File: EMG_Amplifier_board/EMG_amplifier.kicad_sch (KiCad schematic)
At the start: 0 parts

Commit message: add footprints
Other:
- sheet LPF_400Hz ports: added GND; removed none
- sheet first_amp_stage ports: added GND, V_DD/2; removed none
- sheet input_protection_and_decoupling ports: added GND; removed none
- sheet output_protection ports: added GND; removed none

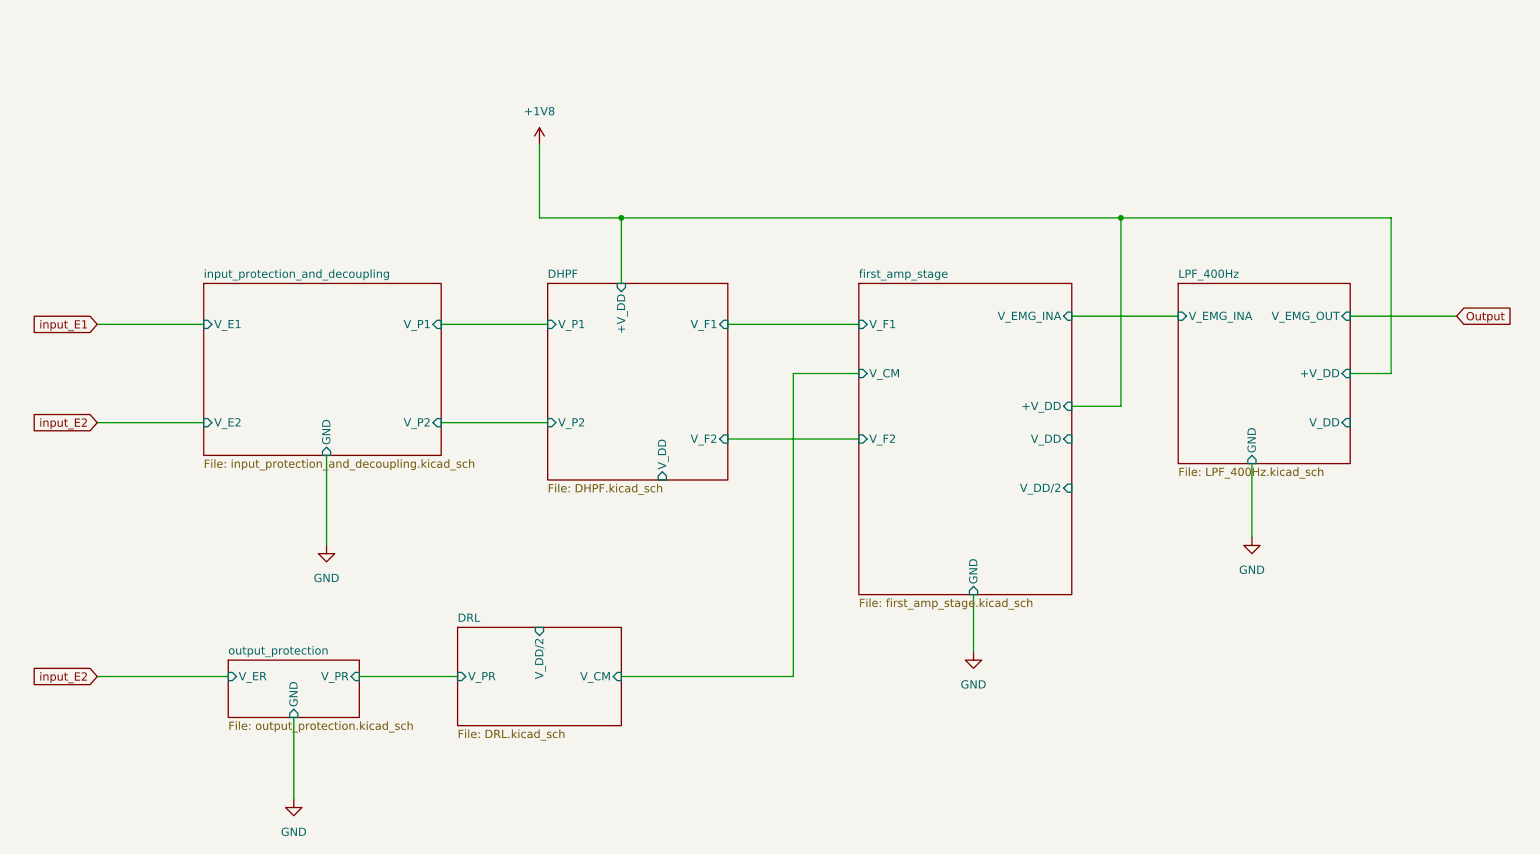
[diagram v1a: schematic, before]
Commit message: update the schematic with shared grounds and pin connectors
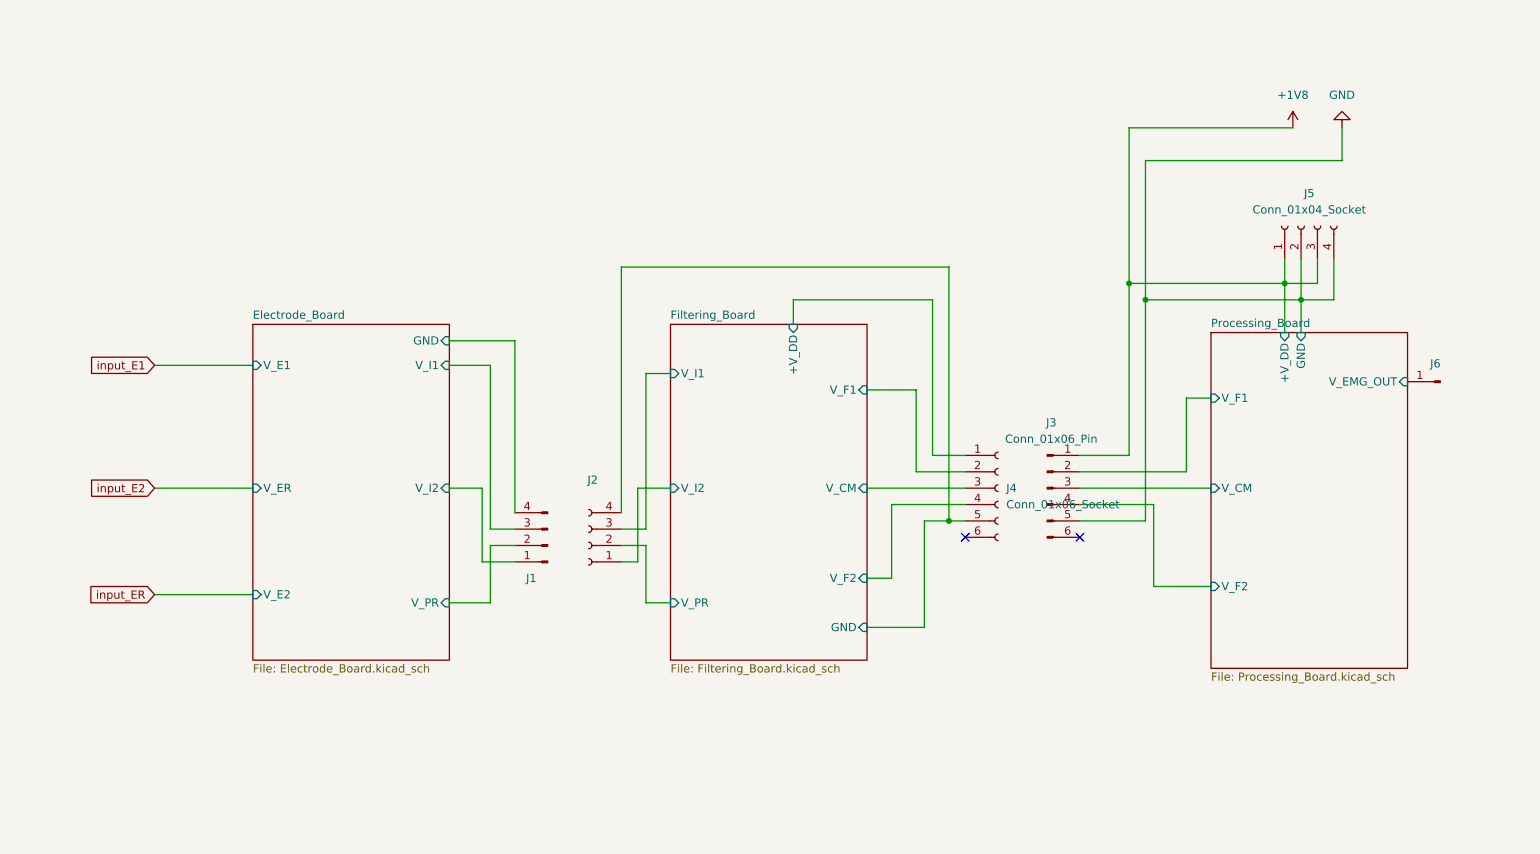
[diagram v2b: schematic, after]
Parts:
- added J1: Conn_01x04_Pin, Connector_PinSocket_2.54mm:PinSocket_2x02_P2.54mm_Vertical, symbol Connector:Conn_01x04_Pin
- added J2, J5: Conn_01x04_Socket, Connector_PinSocket_2.54mm:PinSocket_2x02_P2.54mm_Vertical, symbol Connector:Conn_01x04_Socket
- added J3: Conn_01x06_Pin, Connector_PinHeader_2.54mm:PinHeader_2x03_P2.54mm_Vertical, symbol Connector:Conn_01x06_Pin
- added J4: Conn_01x06_Socket, Connector_PinSocket_2.54mm:PinSocket_2x03_P2.54mm_Vertical, symbol Connector:Conn_01x06_Socket
- added J6: Conn_01x01_Pin, symbol Connector:Conn_01x01_Pin
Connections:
- net +1V8: now also J3.1 (Pin_1), J5.1 (Pin_1), J5.3 (Pin_3)
- net GND: now also J3.5 (Pin_5), J5.2 (Pin_2), J5.4 (Pin_4)
- new net Electrode_Board/GND: J1.4 (Pin_4)
- new net Electrode_Board/V_I1: J1.3 (Pin_3)
- new net Electrode_Board/V_I2: J1.1 (Pin_1)
- new net Electrode_Board/V_PR: J1.2 (Pin_2)
- new net Filtering_Board/+V_DD: J4.1 (Pin_1)
- new net Filtering_Board/GND: J2.4 (Pin_4), J4.5 (Pin_5)
- new net Filtering_Board/V_CM: J4.3 (Pin_3)
- new net Filtering_Board/V_F1: J4.2 (Pin_2)
- new net Filtering_Board/V_F2: J4.4 (Pin_4)
- new net Filtering_Board/V_I1: J2.3 (Pin_3)
- new net Filtering_Board/V_I2: J2.1 (Pin_1)
- new net Filtering_Board/V_PR: J2.2 (Pin_2)
- new net Processing_Board/V_CM: J3.3 (Pin_3)
- new net Processing_Board/V_EMG_OUT: J6.1 (Pin_1)
- new net Processing_Board/V_F1: J3.2 (Pin_2)
- new net Processing_Board/V_F2: J3.4 (Pin_4)
- no-connect marks 0 -> 2
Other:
- removed sheet DHPF
- removed sheet DRL
- removed sheet LPF_400Hz
- removed sheet first_amp_stage
- removed sheet input_protection_and_decoupling
- removed sheet output_protection
- added sheet Electrode_Board (Electrode_Board.kicad_sch)
- added sheet Filtering_Board (Filtering_Board.kicad_sch)
- added sheet Processing_Board (Processing_Board.kicad_sch)

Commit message: pcb design v1
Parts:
- removed J1: Conn_01x04_Pin, Connector_PinSocket_2.54mm:PinSocket_2x02_P2.54mm_Vertical, symbol Connector:Conn_01x04_Pin
- removed J2, J5: Conn_01x04_Socket, Connector_PinSocket_2.54mm:PinSocket_2x02_P2.54mm_Vertical, symbol Connector:Conn_01x04_Socket
- added J1: Conn_01x04_Socket, Connector_PinSocket_2.54mm:PinSocket_2x02_P2.54mm_Vertical, symbol Connector:Conn_01x04_Socket
- added J2: Conn_01x04_Pin, Connector_PinSocket_2.54mm:PinSocket_2x02_P2.54mm_Vertical, symbol Connector:Conn_01x04_Pin
- added J5: Conn_01x04_Pin, Connector_PinHeader_2.54mm:PinHeader_2x02_P2.54mm_Vertical, symbol Connector:Conn_01x04_Pin
- J6: footprint (none) -> Connector_PinHeader_2.54mm:PinHeader_1x01_P2.54mm_Vertical
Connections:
- net Filtering_Board/GND is gone; now on net GND: J4.5 (Pin_5)
- net +1V8: now also J5.2 (Pin_2), J5.4 (Pin_4)
- net Electrode_Board/V_I1: now also J1.2 (Pin_2)
- net Electrode_Board/V_I2: now also J1.4 (Pin_4)
- net Electrode_Board/V_PR: now also J1.3 (Pin_3)
- net Filtering_Board/V_I1: now also J2.2 (Pin_2)
- net Filtering_Board/V_I2: now also J2.4 (Pin_4)
- net Filtering_Board/V_PR: now also J2.3 (Pin_3)
- net GND: now also J1.1 (Pin_1), J2.1 (Pin_1), J5.1 (Pin_1), J5.3 (Pin_3)
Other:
- sheet Electrode_Board ports: added none; removed GND
- sheet Filtering_Board ports: added none; removed GND

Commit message: before working on one-sided design
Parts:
- removed J5: Conn_01x04_Pin, Connector_PinHeader_2.54mm:PinHeader_2x02_P2.54mm_Vertical, symbol Connector:Conn_01x04_Pin
- removed J6: Conn_01x01_Pin, Connector_PinHeader_2.54mm:PinHeader_1x01_P2.54mm_Vertical, symbol Connector:Conn_01x01_Pin
- added J7: Conn_01x06_Pin, Connector_PinHeader_2.54mm:PinHeader_2x03_P2.54mm_Vertical, symbol Connector:Conn_01x06_Pin
- J2: footprint Connector_PinSocket_2.54mm:PinSocket_2x02_P2.54mm_Vertical -> Connector_PinHeader_2.54mm:PinHeader_2x02_P2.54mm_Vertical
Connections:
- net +1V8: now also J7.5 (Pin_5), J7.6 (Pin_6)
- net GND: now also J7.3 (Pin_3), J7.4 (Pin_4)
- net Processing_Board/V_EMG_OUT: now also J7.2 (Pin_2)
- no-connect marks 2 -> 3

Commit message: board V1
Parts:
- added E1: E1, Library:Electrode_Shape, symbol Connector:Conn_01x01_Socket
- added E2: ER, Library:Electrode_Shape, symbol Connector:Conn_01x01_Socket
- added E3: E2, Library:Electrode_Shape, symbol Connector:Conn_01x01_Socket
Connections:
- new net Electrode_Board/V_E1: E1.1 (Pin_1)
- new net Electrode_Board/V_E2: E3.1 (Pin_1)
- new net Electrode_Board/V_ER: E2.1 (Pin_1)
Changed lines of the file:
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@@
-		)
-	)
-	(global_label "input_ER"
-		(shape input)
-		(at 41.91 88.9 180)
-		(fields_autoplaced yes)
-		(effects
-			(font
-				(size 1.27 1.27)
-			)
-			(justify right)
-		)
-		(property "Intersheetrefs" "${INTERSHEET_REFS}"
-			(at 30.7607 88.9 0)
-			(effects
-				(font
-					(size 1.27 1.27)
-				)
-				(justify right)
-				(hide yes)
-			)
-		)
-	)
-	(global_label "input_E2"
-		(shape input)
-		(at 41.91 105.41 180)
-		(fields_autoplaced yes)
-		(effects
-			(font
-				(size 1.27 1.27)
-			)
-			(justify right)
-		)
-		(property "Intersheetrefs" "${INTERSHEET_REFS}"
-			(at 30.8212 105.41 0)
-			(effects
-				(font
-					(size 1.27 1.27)
-				)
-				(justify right)
-				(hide yes)
-			)
-		)
-	)
-	(global_label "input_E1"
-		(shape input)
-		(at 41.91 69.85 180)
-		(fields_autoplaced yes)
-		(effects
-			(font
-				(size 1.27 1.27)
-			)
-			(justify right)
-		)
-		(property "Intersheetrefs" "${INTERSHEET_REFS}"
-			(at 30.8212 69.85 0)
-			(effects
-				(font
-					(size 1.27 1.27)
-				)
-				(justify right)
-				(hide yes)
-			)
 		)
 	)
@@
 	)
 	(symbol
+		(lib_id "Connector:Conn_01x01_Socket")
+		(at 36.83 105.41 180)
+		(unit 1)
+		(exclude_from_sim no)
+		(in_bom yes)
+		(on_board yes)
+		(dnp no)
+		(fields_autoplaced yes)
+		(property "Reference" "E3"
+			(at 37.465 100.33 0)
+			(effects
+				(font
+					(size 1.27 1.27)
+				)
+			)
+		)
+		(property "Value" "E2"
+			(at 37.465 102.87 0)
+			(effects
+				(font
+					(size 1.27 1.27)
+				)
+			)
+		)
+		(property "Footprint" "Library:Electrode_Shape"
+			(at 36.83 105.41 0)
+			(effects
+				(font
+					(size 1.27 1.27)
+				)
+				(hide yes)
+			)
+		)
+		(property "Datasheet" "~"
+			(at 36.83 105.41 0)
+			(effects
+				(font
+					(size 1.27 1.27)
+				)
+				(hide yes)
+			)
+		)
+		(property "Description" "Generic connector, single row, 01x01, script generated"
+			(at 36.83 105.41 0)
+			(effects
+				(font
+					(size 1.27 1.27)
+				)
+				(hide yes)
+			)
+		)
+		(pin "1"
+		)
+		(instances
+			(project "EMG_amplifier"
+				(path "/26861adc-1ddf-4c37-9f8b-8db1c0839771"
+					(reference "E3")
+					(unit 1)
+				)
+			)
+		)
+	)
+	(symbol
 		(lib_id "Connector:Conn_01x06_Pin")
 		(at 224.79 48.26 270)
@@
 					(unit 1)
 				)
+			)
+		)
+	)
+	(symbol
+		(lib_id "Connector:Conn_01x01_Socket")
+		(at 36.83 69.85 180)
+		(unit 1)
+		(exclude_from_sim no)
+		(in_bom yes)
+		(on_board yes)
+		(dnp no)
+		(fields_autoplaced yes)
+		(property "Reference" "E1"
+			(at 37.465 64.77 0)
+			(effects
+				(font
+					(size 1.27 1.27)
+				)
+			)
+		)
+		(property "Value" "E1"
+			(at 37.465 67.31 0)
+			(effects
+				(font
+					(size 1.27 1.27)
+				)
+			)
+		)
+		(property "Footprint" "Library:Electrode_Shape"
+			(at 36.83 69.85 0)
+			(effects
+				(font
+					(size 1.27 1.27)
+				)
+				(hide yes)
+			)
+		)
+		(property "Datasheet" "~"
+			(at 36.83 69.85 0)
+			(effects
+				(font
+					(size 1.27 1.27)
+				)
+				(hide yes)
+			)
+		)
+		(property "Description" "Generic connector, single row, 01x01, script generated"
+			(at 36.83 69.85 0)
+			(effects
+				(font
+					(size 1.27 1.27)
+				)
+				(hide yes)
+			)
+		)
+		(pin "1"
+		)
+		(instances
+			(project ""
+				(path "/26861adc-1ddf-4c37-9f8b-8db1c0839771"
+					(reference "E1")
+					(unit 1)
+				)
+			)
+		)
+	)
+	(symbol
+		(lib_id "Connector:Conn_01x01_Socket")
+		(at 36.83 88.9 180)
+		(unit 1)
+		(exclude_from_sim no)
+		(in_bom yes)
+		(on_board yes)
+		(dnp no)
+		(fields_autoplaced yes)
+		(property "Reference" "E2"
+			(at 37.465 83.82 0)
+			(effects
+				(font
+					(size 1.27 1.27)
+				)
+			)
+		)
+		(property "Value" "ER"
+			(at 37.465 86.36 0)
+			(effects
+				(font
+					(size 1.27 1.27)
+				)
+			)
+		)
+		(property "Footprint" "Library:Electrode_Shape"
+			(at 36.83 88.9 0)
+			(effects
+				(font
+					(size 1.27 1.27)
+				)
+				(hide yes)
+			)
+		)
+		(property "Datasheet" "~"
+			(at 36.83 88.9 0)
+			(effects
+				(font
+					(size 1.27 1.27)
+				)
+				(hide yes)
+			)
+		)
+		(property "Description" "Generic connector, single row, 01x01, script generated"
+			(at 36.83 88.9 0)
+			(effects
+				(font
+					(size 1.27 1.27)
+				)
+				(hide yes)
+			)
+		)
+		(pin "1"
+		)
+		(instances
+			(project "EMG_amplifier"
+				(path "/26861adc-1ddf-4c37-9f8b-8db1c0839771"
+					(reference "E2")
+					(unit 1)
+				)

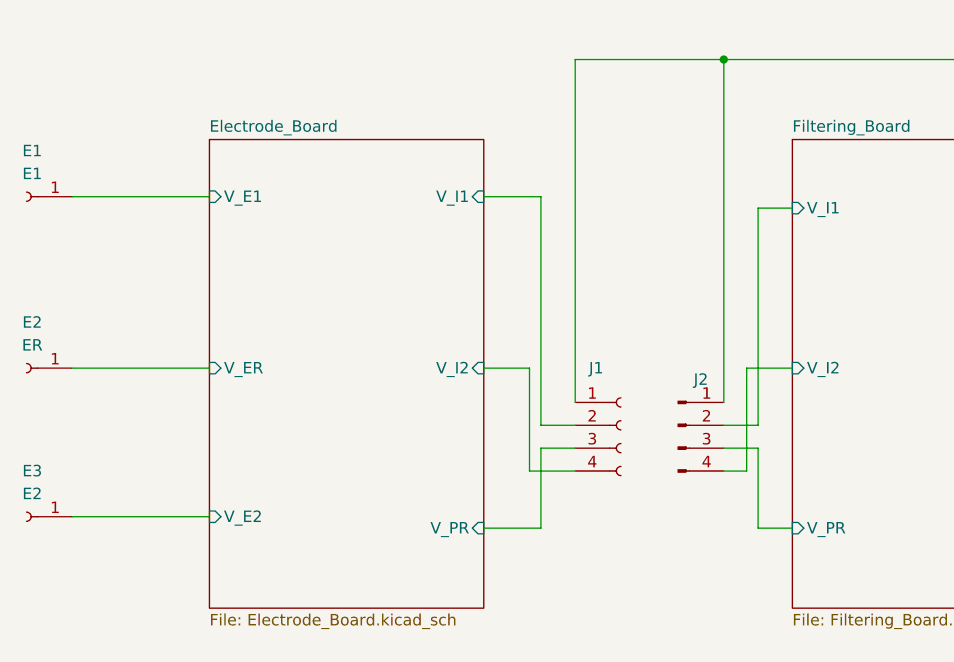
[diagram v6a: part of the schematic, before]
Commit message: add capacitor to ESD
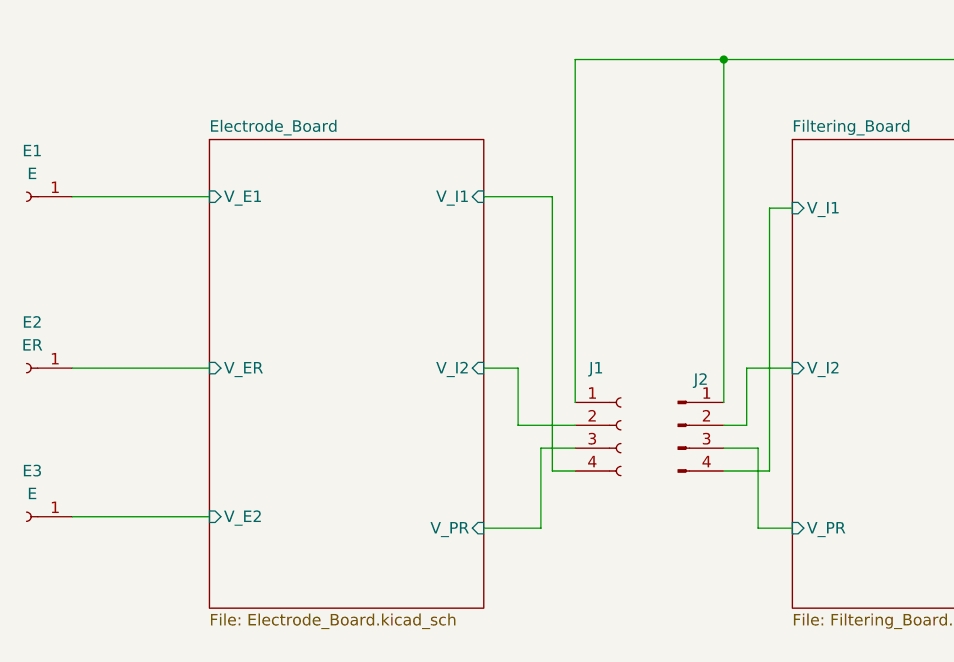
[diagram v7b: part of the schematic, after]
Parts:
- E1: value E1 -> E
- E3: value E2 -> E
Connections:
- net Electrode_Board/V_I1: now also J1.4 (Pin_4); no longer J1.2 (Pin_2)
- net Electrode_Board/V_I2: now also J1.2 (Pin_2); no longer J1.4 (Pin_4)
- net Filtering_Board/V_I1: now also J2.4 (Pin_4); no longer J2.2 (Pin_2)
- net Filtering_Board/V_I2: now also J2.2 (Pin_2); no longer J2.4 (Pin_4)
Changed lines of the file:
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@@
 	(wire
 		(pts
-			(xy 93.98 69.85) (xy 93.98 95.25)
-		)
-		(stroke
-			(width 0)
-			(type default)
-		)
-	)
-	(wire
-		(pts
-			(xy 92.71 100.33) (xy 97.79 100.33)
+			(xy 95.25 69.85) (xy 95.25 100.33)
 		)
 		(stroke
@@
 	(wire
 		(pts
-			(xy 87.63 69.85) (xy 93.98 69.85)
+			(xy 87.63 69.85) (xy 95.25 69.85)
 		)
 		(stroke
@@
 	(wire
 		(pts
+			(xy 91.44 88.9) (xy 91.44 95.25)
+		)
+		(stroke
+			(width 0)
+			(type default)
+		)
+	)
+	(wire
+		(pts
 			(xy 195.58 59.69) (xy 195.58 93.98)
 		)
@@
 	(wire
 		(pts
-			(xy 118.11 95.25) (xy 118.11 71.12)
-		)
-		(stroke
-			(width 0)
-			(type default)
-		)
-	)
-	(wire
-		(pts
-			(xy 87.63 88.9) (xy 92.71 88.9)
+			(xy 119.38 71.12) (xy 119.38 100.33)
+		)
+		(stroke
+			(width 0)
+			(type default)
+		)
+	)
+	(wire
+		(pts
+			(xy 87.63 88.9) (xy 91.44 88.9)
 		)
 		(stroke
@@
 	(wire
 		(pts
-			(xy 116.84 100.33) (xy 114.3 100.33)
-		)
-		(stroke
-			(width 0)
-			(type default)
-		)
-	)
-	(wire
-		(pts
 			(xy 152.4 88.9) (xy 167.64 88.9)
 		)
@@
 	(wire
 		(pts
+			(xy 91.44 95.25) (xy 97.79 95.25)
+		)
+		(stroke
+			(width 0)
+			(type default)
+		)
+	)
+	(wire
+		(pts
 			(xy 226.06 38.1) (xy 195.58 38.1)
 		)
@@
 	(wire
 		(pts
-			(xy 114.3 95.25) (xy 118.11 95.25)
-		)
-		(stroke
-			(width 0)
-			(type default)
-		)
-	)
-	(wire
-		(pts
 			(xy 121.92 106.68) (xy 118.11 106.68)
 		)
@@
 	(wire
 		(pts
-			(xy 92.71 88.9) (xy 92.71 100.33)
+			(xy 95.25 100.33) (xy 97.79 100.33)
 		)
 		(stroke
@@
 	(wire
 		(pts
+			(xy 116.84 95.25) (xy 114.3 95.25)
+		)
+		(stroke
+			(width 0)
+			(type default)
+		)
+	)
+	(wire
+		(pts
 			(xy 162.56 83.82) (xy 162.56 59.69)
 		)
@@
 	(wire
 		(pts
-			(xy 93.98 95.25) (xy 97.79 95.25)
-		)
-		(stroke
-			(width 0)
-			(type default)
-		)
-	)
-	(wire
-		(pts
 			(xy 236.22 72.39) (xy 242.57 72.39)
 		)
@@
 	(wire
 		(pts
-			(xy 116.84 88.9) (xy 116.84 100.33)
+			(xy 119.38 100.33) (xy 114.3 100.33)
 		)
 		(stroke
@@
 	(wire
 		(pts
-			(xy 118.11 71.12) (xy 121.92 71.12)
+			(xy 119.38 71.12) (xy 121.92 71.12)
 		)
 		(stroke
@@
 		(pts
 			(xy 222.25 59.69) (xy 224.79 59.69)
+		)
+		(stroke
+			(width 0)
+			(type default)
+		)
+	)
+	(wire
+		(pts
+			(xy 116.84 88.9) (xy 116.84 95.25)
 		)
 		(stroke
@@
 			)
 		)
-		(property "Value" "E2"
+		(property "Value" "E"
 			(at 37.465 102.87 0)
 			(effects
@@
 			)
 		)
-		(property "Value" "E1"
+		(property "Value" "E"
 			(at 37.465 67.31 0)
 			(effects
